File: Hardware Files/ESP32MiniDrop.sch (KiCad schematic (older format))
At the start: 30 parts, among them J1 0.100\" 2x4 Header, J2 Solenoid1 Terminal, J3 AudioJack3, J4 Barrel_Jack, M1 Conn_01x01, M2 Conn_01x01, M3 Conn_01x01, M4 Conn_01x01, Q1 NMOS 60V 46A, SW1 SPST (BLUE), SW2 SPST (RED), U1 ESP32-WROOM-32, U2 4N25, U3 4N25, U4 AZ1117-3.3

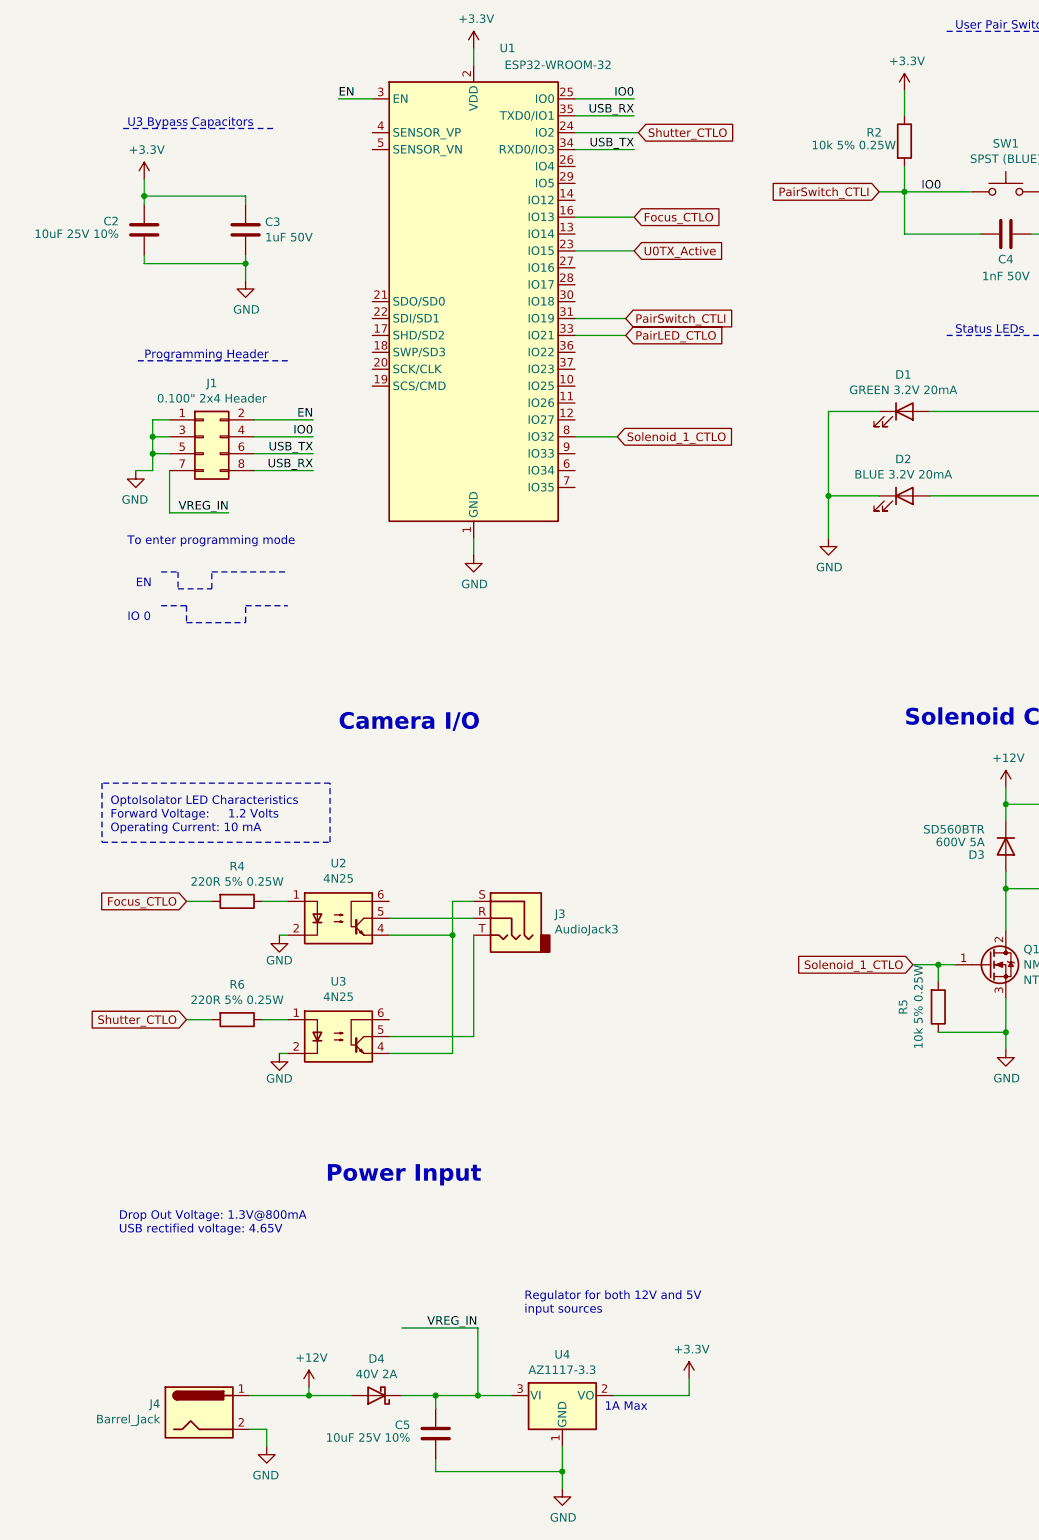
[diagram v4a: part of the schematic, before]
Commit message: Change barrel jack part, update routing
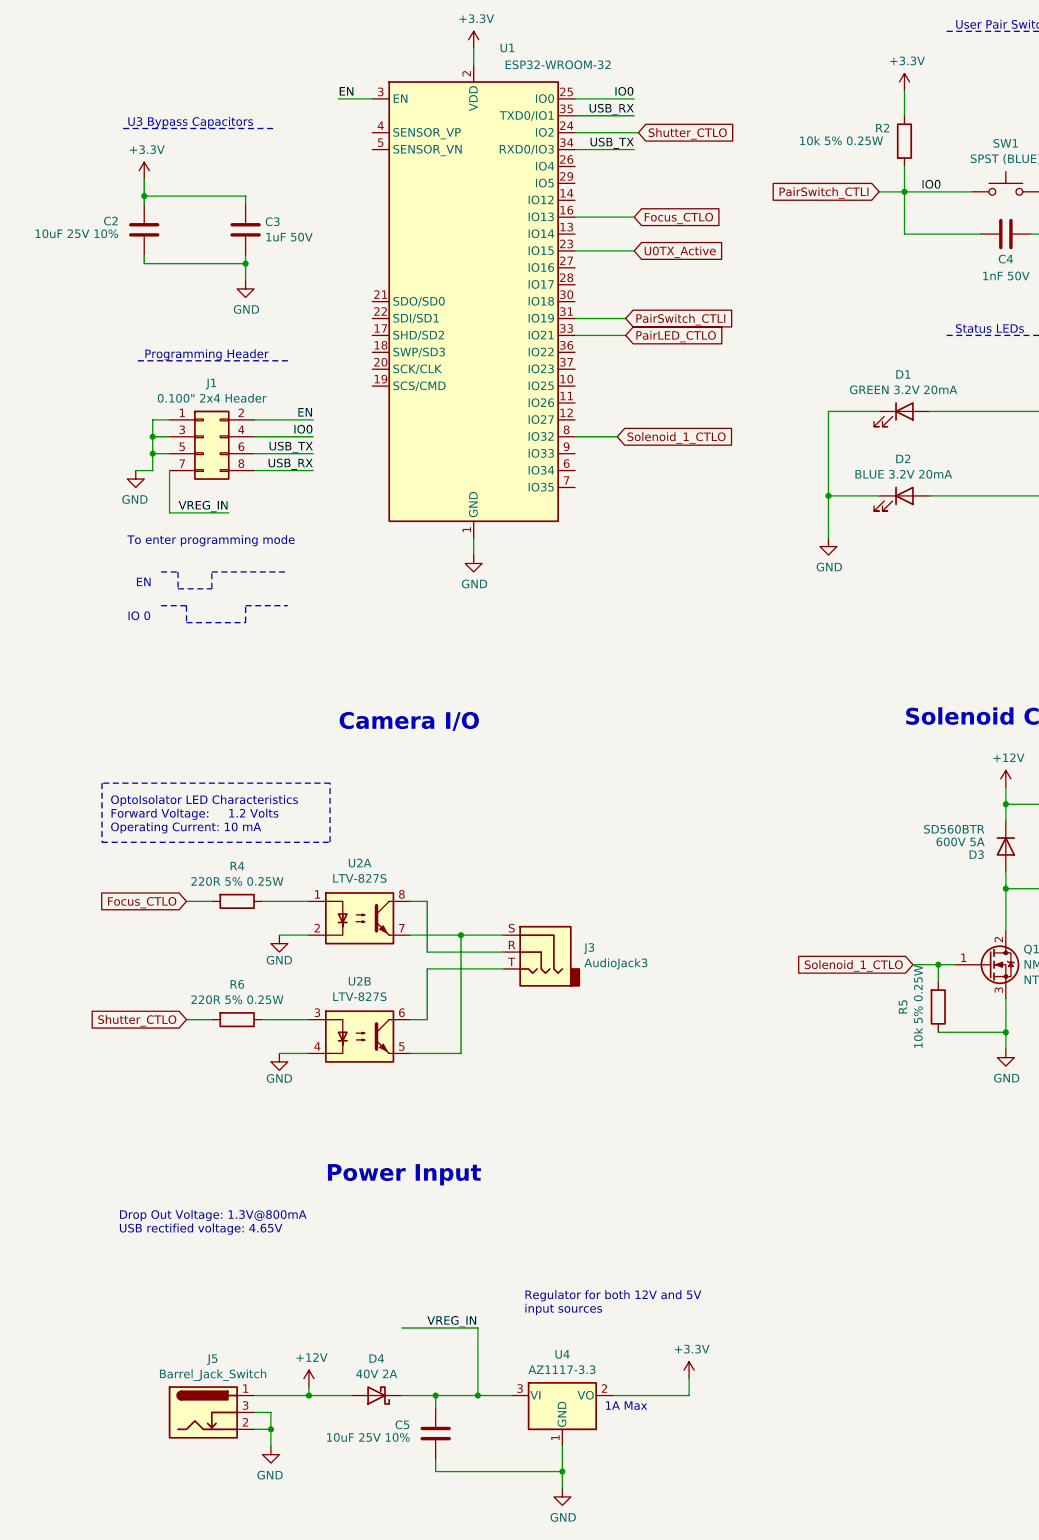
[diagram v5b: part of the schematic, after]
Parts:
- removed J4: Barrel_Jack, ESP32MiniDrop_PCB_Library:PJ-037A, symbol Connector:Barrel_Jack
- removed U2, U3: 4N25, Package_DIP:DIP-6_W8.89mm_SMDSocket_LongPads, symbol Isolator:4N25
- added J5: Barrel_Jack_Switch, Connector_BarrelJack:BarrelJack_Wuerth_6941xx301002, symbol Connector:Barrel_Jack_Switch
- added U2: LTV-827S, Package_DIP:SMDIP-8_W9.53mm, symbol Isolator:LTV-827S
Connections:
- net +12V: now also J5.1
- net GND: now also J5.2, J5.3, U2.2, U2.4
- net at R4.1: now also U2.1
- net at J3.S: now also U2.5, U2.7
- net at J3.R: now also U2.8
- net at J3.T: now also U2.6
- net at R6.1: now also U2.3
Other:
- moved on the sheet: J3
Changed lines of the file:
@@
 User Reset
-$Comp
-L Connector:Barrel_Jack J?
-U 1 1 5F512CA7
-P 1550 9650
-AR Path="/5F45F2B5/5F512CA7" Ref="J?"  Part="1"
-AR Path="/5F512CA7" Ref="J4"  Part="1"
-F 0 "J4" H 1320 9700 50  0000 R CNN
-F 1 "Barrel_Jack" H 1320 9609 50  0000 R CNN
-F 2 "ESP32MiniDrop_PCB_Library:PJ-037A" H 1600 9610 50  0001 C CNN
-F 3 "" H 1600 9610 50  0001 C CNN
-F 4 "CUI Devices" H 1550 9650 50  0001 C CNN "MF"
-F 5 "PJ-037A" H 1550 9650 50  0001 C CNN "MPN"
-	1    1550 9650
-	1    0    0    -1
-$EndComp
-Wire Wire Line
-	1850 9750 1950 9750
-Wire Wire Line
-	1950 9750 1950 9850
-$Comp
-L power:GND #PWR?
-U 1 1 5F512CAF
-P 1950 9850
-AR Path="/5F45F2B5/5F512CAF" Ref="#PWR?"  Part="1"
-AR Path="/5F512CAF" Ref="#PWR020"  Part="1"
-F 0 "#PWR020" H 1950 9600 50  0001 C CNN
-F 1 "GND" H 1955 9677 50  0000 C CNN
-F 2 "" H 1950 9850 50  0001 C CNN
-F 3 "" H 1950 9850 50  0001 C CNN
-	1    1950 9850
-	-1   0    0    -1
-$EndComp
-Connection ~ 2200 9550
-Wire Wire Line
-	1850 9550 2200 9550
 $Comp
 L Device:C C?
@@
 AR Path="/5F45F2B5/5F512D48" Ref="R?"  Part="1"
 AR Path="/5F512D48" Ref="R2"  Part="1"
-F 0 "R2" H 5500 2175 50  0000 L CNN
-F 1 "10k 5% 0.25W" H 5175 2100 50  0000 L CNN
+F 0 "R2" H 5550 2200 50  0000 L CNN
+F 1 "10k 5% 0.25W" H 5100 2125 50  0000 L CNN
 F 2 "Resistor_SMD:R_1206_3216Metric_Pad1.42x1.75mm_HandSolder" V 5655 2125 50  0001 C CNN
 F 3 "~" H 5725 2125 50  0001 C CNN
@@
 Drop Out Voltage: 1.3V@800mA\nUSB rectified voltage: 4.65V
 $Comp
-L Isolator:4N25 U?
-U 1 1 5F5C6C58
-P 2375 6725
-AR Path="/5F5BF78E/5F5C6C58" Ref="U?"  Part="1"
-AR Path="/5F5C6C58" Ref="U2"  Part="1"
-F 0 "U2" H 2375 7050 50  0000 C CNN
-F 1 "4N25" H 2375 6959 50  0000 C CNN
-F 2 "Package_DIP:DIP-6_W8.89mm_SMDSocket_LongPads" H 2175 6525 50  0001 L CIN
-F 3 "https://www.vishay.com/docs/83725/4n25.pdf" H 2375 6725 50  0001 L CNN
-F 4 "Broadcom Limited" H 2375 6725 50  0001 C CNN "MF"
-F 5 "4N25-500E" H 2375 6725 50  0001 C CNN "MPN"
-	1    2375 6725
-	1    0    0    -1
-$EndComp
-$Comp
 L Connector:AudioJack3 J?
 U 1 1 5F5C6C60
-P 3375 6725
+P 3550 6925
 AR Path="/5F5BF78E/5F5C6C60" Ref="J?"  Part="1"
 AR Path="/5F5C6C60" Ref="J3"  Part="1"
-F 0 "J3" H 3095 6750 50  0000 R CNN
-F 1 "AudioJack3" H 3095 6659 50  0000 R CNN
-F 2 "ESP32MiniDrop_PCB_Library:STX-3000" H 3375 6725 50  0001 C CNN
-F 3 "~" H 3375 6725 50  0001 C CNN
-F 4 "Kycon, Inc." H 3375 6725 50  0001 C CNN "MF"
-F 5 "STX-3000" H 3375 6725 50  0001 C CNN "MPN"
-	1    3375 6725
+F 0 "J3" H 3270 6950 50  0000 R CNN
+F 1 "AudioJack3" H 3270 6859 50  0000 R CNN
+F 2 "ESP32MiniDrop_PCB_Library:STX-3000" H 3550 6925 50  0001 C CNN
+F 3 "~" H 3550 6925 50  0001 C CNN
+F 4 "Kycon, Inc." H 3550 6925 50  0001 C CNN "MF"
+F 5 "STX-3000" H 3550 6925 50  0001 C CNN "MPN"
+	1    3550 6925
 	-1   0    0    -1
-$EndComp
-$Comp
-L Isolator:4N25 U?
-U 1 1 5F5C6C68
-P 2375 7425
-AR Path="/5F5BF78E/5F5C6C68" Ref="U?"  Part="1"
-AR Path="/5F5C6C68" Ref="U3"  Part="1"
-F 0 "U3" H 2375 7750 50  0000 C CNN
-F 1 "4N25" H 2375 7659 50  0000 C CNN
-F 2 "Package_DIP:DIP-6_W8.89mm_SMDSocket_LongPads" H 2175 7225 50  0001 L CIN
-F 3 "https://www.vishay.com/docs/83725/4n25.pdf" H 2375 7425 50  0001 L CNN
-F 4 "Broadcom Limited" H 2375 7425 50  0001 C CNN "MF"
-F 5 "4N25-500E" H 2375 7425 50  0001 C CNN "MPN"
-	1    2375 7425
-	1    0    0    -1
 $EndComp
 Text GLabel 1475 7325 0    50   Input ~ 0
@@
 $EndComp
 Wire Wire Line
-	1925 6625 2075 6625
-Wire Wire Line
 	1475 6625 1625 6625
 $Comp
@@
 Wire Wire Line
 	1475 7325 1625 7325
-Wire Wire Line
-	1925 7325 2075 7325
 $Comp
 L power:GND #PWR?
@@
 	1    0    0    -1
 $EndComp
-Wire Wire Line
-	2025 6825 2075 6825
 $Comp
 L power:GND #PWR?
@@
 	1    0    0    -1
 $EndComp
-Wire Wire Line
-	2025 7525 2075 7525
 Text Notes 1025 6225 0    50   ~ 0
 OptoIsolator LED Characteristics\nForward Voltage:     1.2 Volts\nOperating Current: 10 mA
@@
 Wire Notes Line
 	9200 1975 9675 1975
-Wire Wire Line
-	3050 7525 3050 6825
-Wire Wire Line
-	2675 7525 3050 7525
-Wire Wire Line
-	3175 6625 3050 6625
-Wire Wire Line
-	3050 6625 3050 6825
-Connection ~ 3050 6825
-Wire Wire Line
-	2675 6825 3050 6825
-Wire Wire Line
-	2675 6725 3175 6725
-Wire Wire Line
-	3175 6825 3175 7425
-Wire Wire Line
-	3175 7425 2675 7425
 Wire Wire Line
 	3775 3875 4025 3875
@@
 Wire Wire Line
 	3700 10000 3700 10100
+$Comp
+L Isolator:LTV-827S U2
+U 2 1 5F7A6142
+P 2500 7425
+F 0 "U2" H 2500 7750 50  0000 C CNN
+F 1 "LTV-827S" H 2500 7659 50  0000 C CNN
+F 2 "Package_DIP:SMDIP-8_W9.53mm" H 2500 7125 50  0001 C CNN
+F 3 "http://www.us.liteon.com/downloads/LTV-817-827-847.PDF" H 1700 7975 50  0001 C CNN
+	2    2500 7425
+	1    0    0    -1
+$EndComp
+$Comp
+L Isolator:LTV-827S U2
+U 1 1 5F7A5EFB
+P 2500 6725
+F 0 "U2" H 2500 7050 50  0000 C CNN
+F 1 "LTV-827S" H 2500 6959 50  0000 C CNN
+F 2 "Package_DIP:SMDIP-8_W9.53mm" H 2500 6425 50  0001 C CNN
+F 3 "http://www.us.liteon.com/downloads/LTV-817-827-847.PDF" H 1700 7275 50  0001 C CNN
+	1    2500 6725
+	1    0    0    -1
+$EndComp
+Wire Wire Line
+	2800 6825 3100 6825
+Connection ~ 3100 6825
+Wire Wire Line
+	3100 6825 3350 6825
+Wire Wire Line
+	2800 6625 2900 6625
+Wire Wire Line
+	2900 6625 2900 6925
+Wire Wire Line
+	2900 6925 3350 6925
+Wire Wire Line
+	2900 7025 3350 7025
+Wire Wire Line
+	1925 7325 2200 7325
+Wire Wire Line
+	2025 7525 2200 7525
+Wire Wire Line
+	1925 6625 2200 6625
+Wire Wire Line
+	2025 6825 2200 6825
+Wire Wire Line
+	2800 7325 2900 7325
+Wire Wire Line
+	2900 7025 2900 7325
+Wire Wire Line
+	2800 7525 3100 7525
+Wire Wire Line
+	3100 6825 3100 7525
+$Comp
+L Connector:Barrel_Jack_Switch J5
+U 1 1 5F8144D0
+P 1575 9650
+F 0 "J5" H 1632 9967 50  0000 C CNN
+F 1 "Barrel_Jack_Switch" H 1632 9876 50  0000 C CNN
+F 2 "Connector_BarrelJack:BarrelJack_Wuerth_6941xx301002" H 1625 9610 50  0001 C CNN
+F 3 "~" H 1625 9610 50  0001 C CNN
+	1    1575 9650
+	1    0    0    -1
+$EndComp
+$Comp
+L power:GND #PWR?
+U 1 1 5F815BAF
+P 1975 9850
+AR Path="/5F45F2B5/5F815BAF" Ref="#PWR?"  Part="1"
+AR Path="/5F815BAF" Ref="#PWR0101"  Part="1"
+F 0 "#PWR0101" H 1975 9600 50  0001 C CNN
+F 1 "GND" H 1980 9677 50  0000 C CNN
+F 2 "" H 1975 9850 50  0001 C CNN
+F 3 "" H 1975 9850 50  0001 C CNN
+	1    1975 9850
+	-1   0    0    -1
+$EndComp
+Wire Wire Line
+	1875 9650 1975 9650
+Wire Wire Line
+	1975 9650 1975 9750
+Wire Wire Line
+	1875 9750 1975 9750
+Connection ~ 1975 9750
+Wire Wire Line
+	1975 9750 1975 9850
+Wire Wire Line
+	1875 9550 2200 9550
+Connection ~ 2200 9550
 $EndSCHEMATC
